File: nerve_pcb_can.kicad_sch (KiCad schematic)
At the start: 4 parts, among them J10 CAN1, J9 CAN1

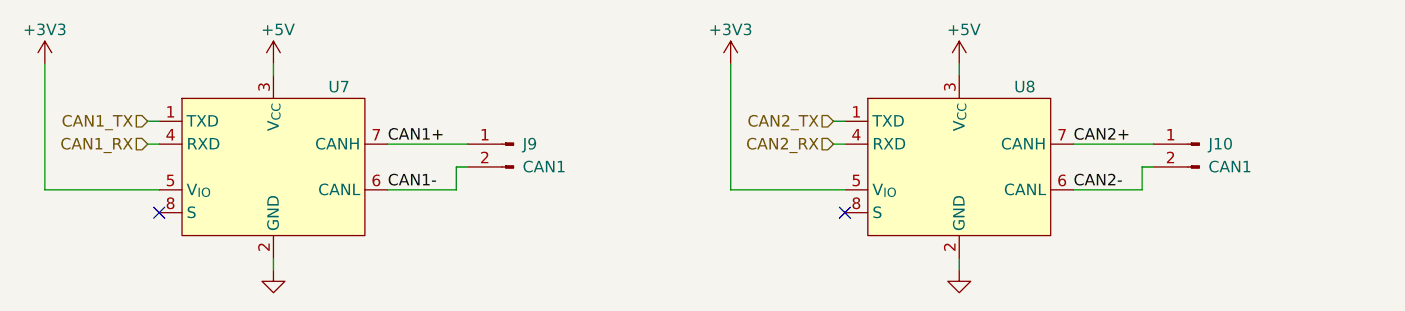
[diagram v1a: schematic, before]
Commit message: Add schematic changes from PCB routing/layout
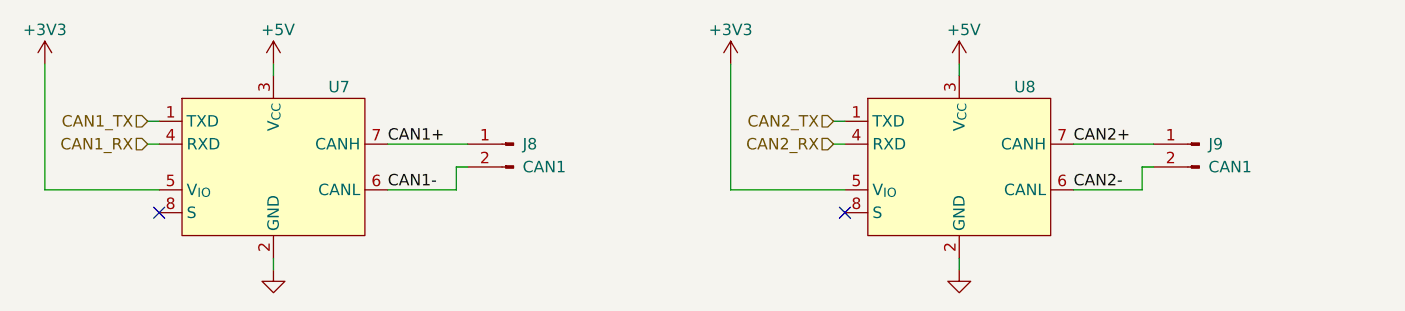
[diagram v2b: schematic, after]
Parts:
- renumbered J9 to J8, J10 to J9
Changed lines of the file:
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@@
 		(dnp no)
 		(fields_autoplaced yes)
-		(property "Reference" "#PWR067"
+		(property "Reference" "#PWR065"
 			(at 111.76 127 0)
 			(effects
@@
 			(project "nerve_pcb"
 				(path "/c0277862-b3f2-4e0e-986f-34702f0543f0/4fcd2c12-d66e-4aef-b6ae-64082d99e104"
-					(reference "#PWR067")
+					(reference "#PWR065")
 					(unit 1)
 				)
@@
 		(on_board yes)
 		(dnp no)
-		(property "Reference" "#PWR063"
+		(property "Reference" "#PWR061"
 			(at 86.36 101.6 0)
 			(effects
@@
 			(project "nerve_pcb"
 				(path "/c0277862-b3f2-4e0e-986f-34702f0543f0/4fcd2c12-d66e-4aef-b6ae-64082d99e104"
-					(reference "#PWR063")
+					(reference "#PWR061")
 					(unit 1)
 				)
@@
 		(on_board yes)
 		(dnp no)
-		(property "Reference" "#PWR064"
+		(property "Reference" "#PWR062"
 			(at 111.76 101.6 0)
 			(effects
@@
 			(project "nerve_pcb"
 				(path "/c0277862-b3f2-4e0e-986f-34702f0543f0/4fcd2c12-d66e-4aef-b6ae-64082d99e104"
-					(reference "#PWR064")
+					(reference "#PWR062")
 					(unit 1)
 				)
@@
 		(on_board yes)
 		(dnp no)
-		(property "Reference" "#PWR065"
+		(property "Reference" "#PWR063"
 			(at 162.56 101.6 0)
 			(effects
@@
 			(project "nerve_pcb"
 				(path "/c0277862-b3f2-4e0e-986f-34702f0543f0/4fcd2c12-d66e-4aef-b6ae-64082d99e104"
-					(reference "#PWR065")
+					(reference "#PWR063")
 					(unit 1)
 				)
@@
 		(on_board yes)
 		(dnp no)
-		(property "Reference" "#PWR066"
+		(property "Reference" "#PWR064"
 			(at 187.96 101.6 0)
 			(effects
@@
 			(project "nerve_pcb"
 				(path "/c0277862-b3f2-4e0e-986f-34702f0543f0/4fcd2c12-d66e-4aef-b6ae-64082d99e104"
-					(reference "#PWR066")
+					(reference "#PWR064")
 					(unit 1)
 				)
@@
 		(on_board yes)
 		(dnp no)
-		(property "Reference" "J9"
+		(property "Reference" "J8"
 			(at 139.446 106.68 0)
 			(effects
@@
 			(project "nerve_pcb"
 				(path "/c0277862-b3f2-4e0e-986f-34702f0543f0/4fcd2c12-d66e-4aef-b6ae-64082d99e104"
-					(reference "J9")
+					(reference "J8")
 					(unit 1)
 				)
@@
 		(on_board yes)
 		(dnp no)
-		(property "Reference" "J10"
+		(property "Reference" "J9"
 			(at 215.646 106.68 0)
 			(effects
@@
 			(project "nerve_pcb"
 				(path "/c0277862-b3f2-4e0e-986f-34702f0543f0/4fcd2c12-d66e-4aef-b6ae-64082d99e104"
-					(reference "J10")
+					(reference "J9")
 					(unit 1)
 				)
@@
 		(dnp no)
 		(fields_autoplaced yes)
-		(property "Reference" "#PWR068"
+		(property "Reference" "#PWR066"
 			(at 187.96 127 0)
 			(effects
@@
 			(project "nerve_pcb"
 				(path "/c0277862-b3f2-4e0e-986f-34702f0543f0/4fcd2c12-d66e-4aef-b6ae-64082d99e104"
-					(reference "#PWR068")
-					(unit 1)
-				)
+					(reference "#PWR066")
+					(unit 1)
+				)

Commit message: Update refs on schematics
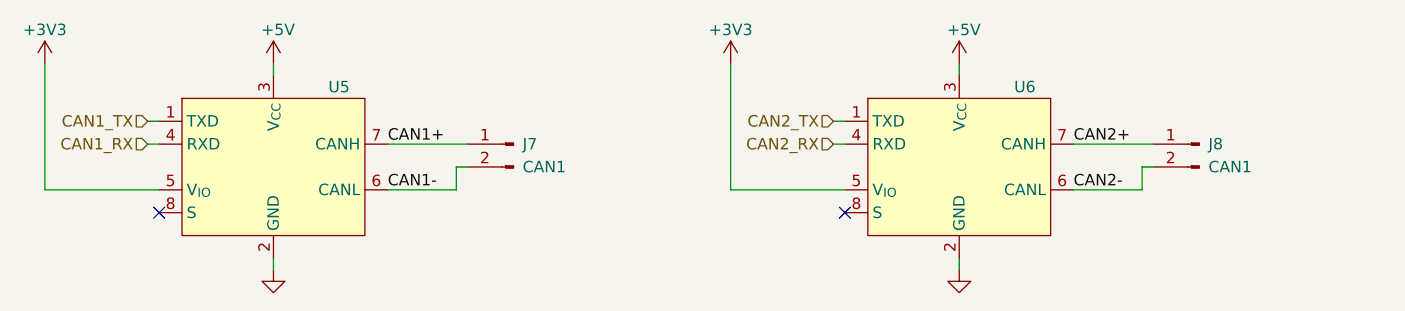
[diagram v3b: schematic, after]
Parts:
- renumbered J8 to J7, J9 to J8, U7 to U5, U8 to U6
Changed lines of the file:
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@@
 		(dnp no)
 		(fields_autoplaced yes)
-		(property "Reference" "#PWR065"
+		(property "Reference" "#PWR081"
 			(at 111.76 127 0)
 			(effects
@@
 			(project "nerve_pcb"
 				(path "/c0277862-b3f2-4e0e-986f-34702f0543f0/4fcd2c12-d66e-4aef-b6ae-64082d99e104"
-					(reference "#PWR065")
+					(reference "#PWR081")
 					(unit 1)
 				)
@@
 		(on_board yes)
 		(dnp no)
-		(property "Reference" "#PWR061"
+		(property "Reference" "#PWR077"
 			(at 86.36 101.6 0)
 			(effects
@@
 			(project "nerve_pcb"
 				(path "/c0277862-b3f2-4e0e-986f-34702f0543f0/4fcd2c12-d66e-4aef-b6ae-64082d99e104"
-					(reference "#PWR061")
+					(reference "#PWR077")
 					(unit 1)
 				)
@@
 		(on_board yes)
 		(dnp no)
-		(property "Reference" "U8"
+		(property "Reference" "U6"
 			(at 194.056 100.33 0)
 			(effects
@@
 			(project "nerve_pcb"
 				(path "/c0277862-b3f2-4e0e-986f-34702f0543f0/4fcd2c12-d66e-4aef-b6ae-64082d99e104"
-					(reference "U8")
+					(reference "U6")
 					(unit 1)
 				)
@@
 		(on_board yes)
 		(dnp no)
-		(property "Reference" "#PWR062"
+		(property "Reference" "#PWR078"
 			(at 111.76 101.6 0)
 			(effects
@@
 			(project "nerve_pcb"
 				(path "/c0277862-b3f2-4e0e-986f-34702f0543f0/4fcd2c12-d66e-4aef-b6ae-64082d99e104"
-					(reference "#PWR062")
+					(reference "#PWR078")
 					(unit 1)
 				)
@@
 		(on_board yes)
 		(dnp no)
-		(property "Reference" "#PWR063"
+		(property "Reference" "#PWR079"
 			(at 162.56 101.6 0)
 			(effects
@@
 			(project "nerve_pcb"
 				(path "/c0277862-b3f2-4e0e-986f-34702f0543f0/4fcd2c12-d66e-4aef-b6ae-64082d99e104"
-					(reference "#PWR063")
+					(reference "#PWR079")
 					(unit 1)
 				)
@@
 		(on_board yes)
 		(dnp no)
-		(property "Reference" "#PWR064"
+		(property "Reference" "#PWR080"
 			(at 187.96 101.6 0)
 			(effects
@@
 			(project "nerve_pcb"
 				(path "/c0277862-b3f2-4e0e-986f-34702f0543f0/4fcd2c12-d66e-4aef-b6ae-64082d99e104"
-					(reference "#PWR064")
+					(reference "#PWR080")
 					(unit 1)
 				)
@@
 		(on_board yes)
 		(dnp no)
-		(property "Reference" "U7"
+		(property "Reference" "U5"
 			(at 117.856 100.33 0)
 			(effects
@@
 			(project ""
 				(path "/c0277862-b3f2-4e0e-986f-34702f0543f0/4fcd2c12-d66e-4aef-b6ae-64082d99e104"
-					(reference "U7")
+					(reference "U5")
 					(unit 1)
 				)
@@
 		(on_board yes)
 		(dnp no)
-		(property "Reference" "J8"
+		(property "Reference" "J7"
 			(at 139.446 106.68 0)
 			(effects
@@
 			(project "nerve_pcb"
 				(path "/c0277862-b3f2-4e0e-986f-34702f0543f0/4fcd2c12-d66e-4aef-b6ae-64082d99e104"
-					(reference "J8")
+					(reference "J7")
 					(unit 1)
 				)
@@
 		(on_board yes)
 		(dnp no)
-		(property "Reference" "J9"
+		(property "Reference" "J8"
 			(at 215.646 106.68 0)
 			(effects
@@
 			(project "nerve_pcb"
 				(path "/c0277862-b3f2-4e0e-986f-34702f0543f0/4fcd2c12-d66e-4aef-b6ae-64082d99e104"
-					(reference "J9")
+					(reference "J8")
 					(unit 1)
 				)
@@
 		(dnp no)
 		(fields_autoplaced yes)
-		(property "Reference" "#PWR066"
+		(property "Reference" "#PWR082"
 			(at 187.96 127 0)
 			(effects
@@
 			(project "nerve_pcb"
 				(path "/c0277862-b3f2-4e0e-986f-34702f0543f0/4fcd2c12-d66e-4aef-b6ae-64082d99e104"
-					(reference "#PWR066")
-					(unit 1)
-				)
+					(reference "#PWR082")
+					(unit 1)
+				)

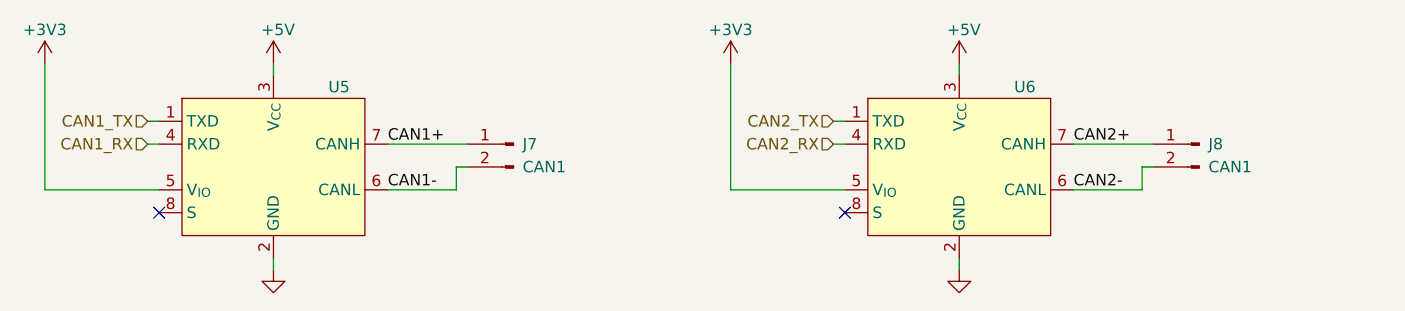
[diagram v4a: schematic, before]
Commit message: Clean up schematics and ensure PCB parity
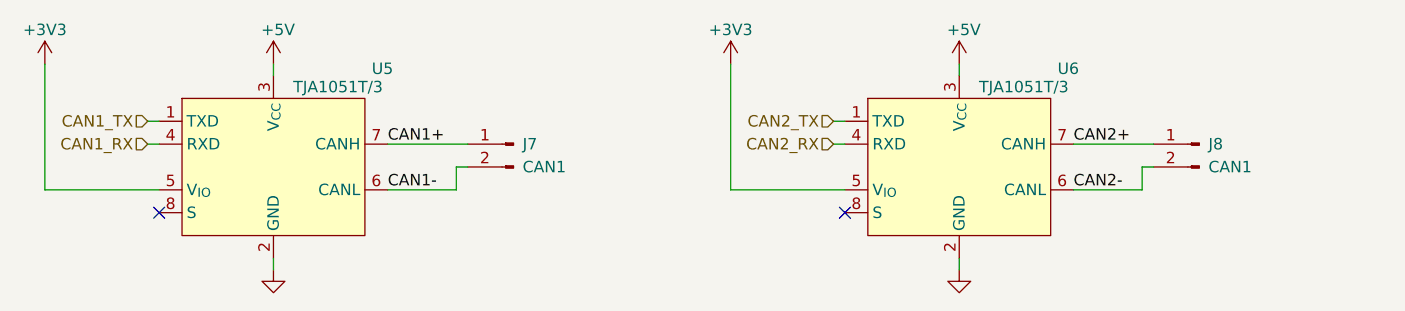
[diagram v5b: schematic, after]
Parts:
- U5, U6: value ~ -> TJA1051T/3
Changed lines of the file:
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@@
 		(dnp no)
 		(property "Reference" "U6"
-			(at 194.056 100.33 0)
+			(at 198.882 98.298 0)
 			(effects
 				(font
@@
 			)
 		)
-		(property "Value" "~"
+		(property "Value" "TJA1051T/3"
 			(at 190.1541 100.33 0)
 			(effects
@@
 		(dnp no)
 		(property "Reference" "U5"
-			(at 117.856 100.33 0)
+			(at 122.682 98.298 0)
 			(effects
 				(font
@@
 			)
 		)
-		(property "Value" "~"
+		(property "Value" "TJA1051T/3"
 			(at 113.9541 100.33 0)
 			(effects

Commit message: Add CAN 120ohm resistors
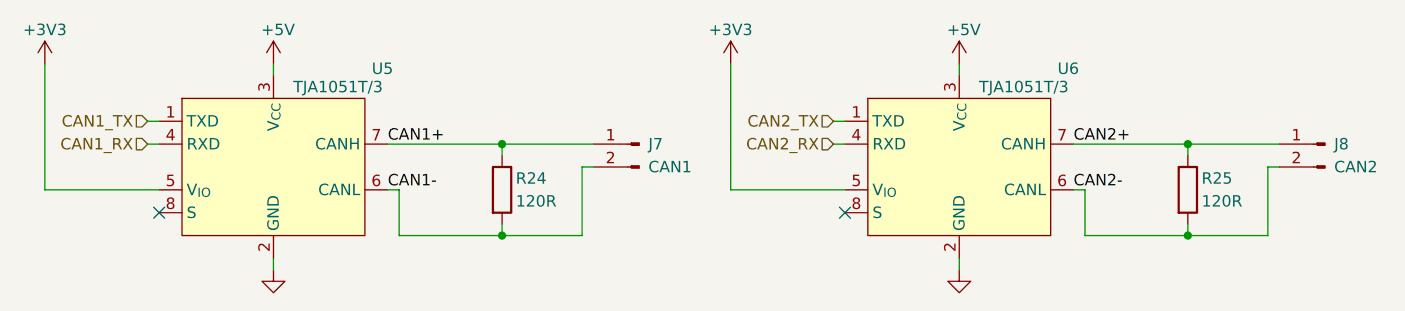
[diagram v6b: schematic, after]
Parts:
- added R24, R25: 120R, Resistor_SMD:R_0603_1608Metric, symbol Device:R
- J8: value CAN1 -> CAN2
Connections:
- net CAN1+: now also R24.1
- net CAN1-: now also R24.2
- net CAN2+: now also R25.1
- net CAN2-: now also R25.2
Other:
- moved on the sheet: J7, J8

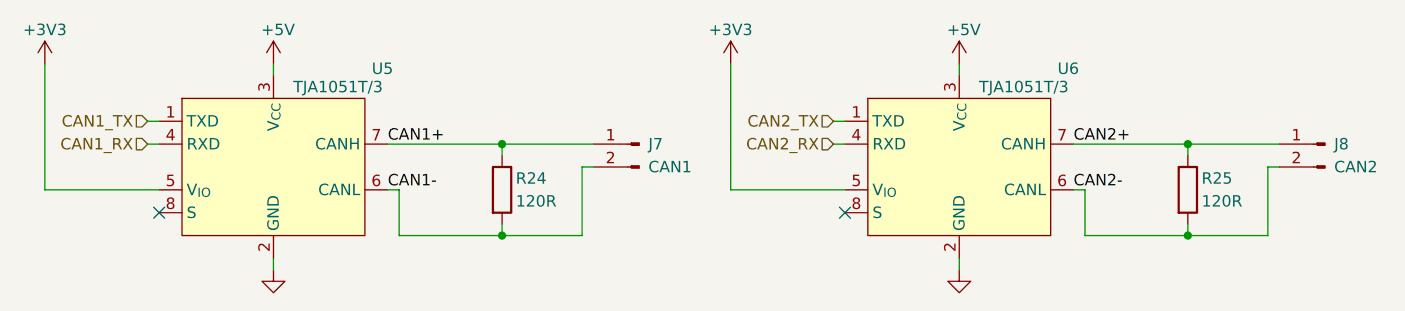
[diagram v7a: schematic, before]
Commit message: Schematic corrections
- Add decoupling caps for sensor ICs
- Fix clock circuits
- Add BNO085 clock jumper
- Minor cleanup
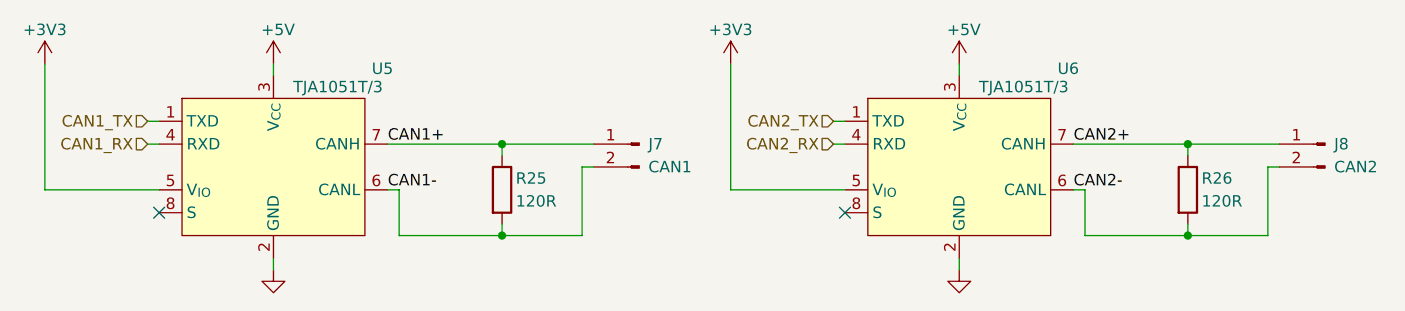
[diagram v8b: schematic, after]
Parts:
- renumbered R24 to R25, R25 to R26
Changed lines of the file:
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@@
 		(dnp no)
 		(fields_autoplaced yes)
-		(property "Reference" "#PWR082"
+		(property "Reference" "#PWR083"
 			(at 111.76 127 0)
 			(effects
@@
 			(project "nerve_pcb"
 				(path "/c0277862-b3f2-4e0e-986f-34702f0543f0/4fcd2c12-d66e-4aef-b6ae-64082d99e104"
-					(reference "#PWR082")
+					(reference "#PWR083")
 					(unit 1)
 				)
@@
 		(on_board yes)
 		(dnp no)
-		(property "Reference" "#PWR078"
+		(property "Reference" "#PWR079"
 			(at 86.36 101.6 0)
 			(effects
@@
 			(project "nerve_pcb"
 				(path "/c0277862-b3f2-4e0e-986f-34702f0543f0/4fcd2c12-d66e-4aef-b6ae-64082d99e104"
-					(reference "#PWR078")
+					(reference "#PWR079")
 					(unit 1)
 				)
@@
 		(on_board yes)
 		(dnp no)
-		(property "Reference" "R24"
+		(property "Reference" "R25"
 			(at 138.684 110.49 0)
 			(effects
@@
 			(project "nerve_pcb"
 				(path "/c0277862-b3f2-4e0e-986f-34702f0543f0/4fcd2c12-d66e-4aef-b6ae-64082d99e104"
-					(reference "R24")
+					(reference "R25")
 					(unit 1)
 				)
@@
 		(on_board yes)
 		(dnp no)
-		(property "Reference" "#PWR079"
+		(property "Reference" "#PWR080"
 			(at 111.76 101.6 0)
 			(effects
@@
 			(project "nerve_pcb"
 				(path "/c0277862-b3f2-4e0e-986f-34702f0543f0/4fcd2c12-d66e-4aef-b6ae-64082d99e104"
-					(reference "#PWR079")
+					(reference "#PWR080")
 					(unit 1)
 				)
@@
 		(on_board yes)
 		(dnp no)
-		(property "Reference" "#PWR080"
+		(property "Reference" "#PWR081"
 			(at 162.56 101.6 0)
 			(effects
@@
 			(project "nerve_pcb"
 				(path "/c0277862-b3f2-4e0e-986f-34702f0543f0/4fcd2c12-d66e-4aef-b6ae-64082d99e104"
-					(reference "#PWR080")
+					(reference "#PWR081")
 					(unit 1)
 				)
@@
 		(on_board yes)
 		(dnp no)
-		(property "Reference" "#PWR081"
+		(property "Reference" "#PWR082"
 			(at 187.96 101.6 0)
 			(effects
@@
 			(project "nerve_pcb"
 				(path "/c0277862-b3f2-4e0e-986f-34702f0543f0/4fcd2c12-d66e-4aef-b6ae-64082d99e104"
-					(reference "#PWR081")
+					(reference "#PWR082")
 					(unit 1)
 				)
@@
 		(on_board yes)
 		(dnp no)
-		(property "Reference" "R25"
+		(property "Reference" "R26"
 			(at 214.884 110.49 0)
 			(effects
@@
 			(project "nerve_pcb"
 				(path "/c0277862-b3f2-4e0e-986f-34702f0543f0/4fcd2c12-d66e-4aef-b6ae-64082d99e104"
-					(reference "R25")
+					(reference "R26")
 					(unit 1)
 				)
@@
 		(dnp no)
 		(fields_autoplaced yes)
-		(property "Reference" "#PWR083"
+		(property "Reference" "#PWR084"
 			(at 187.96 127 0)
 			(effects
@@
 			(project "nerve_pcb"
 				(path "/c0277862-b3f2-4e0e-986f-34702f0543f0/4fcd2c12-d66e-4aef-b6ae-64082d99e104"
-					(reference "#PWR083")
-					(unit 1)
-				)
+					(reference "#PWR084")
+					(unit 1)
+				)
